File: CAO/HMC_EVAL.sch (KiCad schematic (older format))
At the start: 36 parts, among them U1 OPA2209

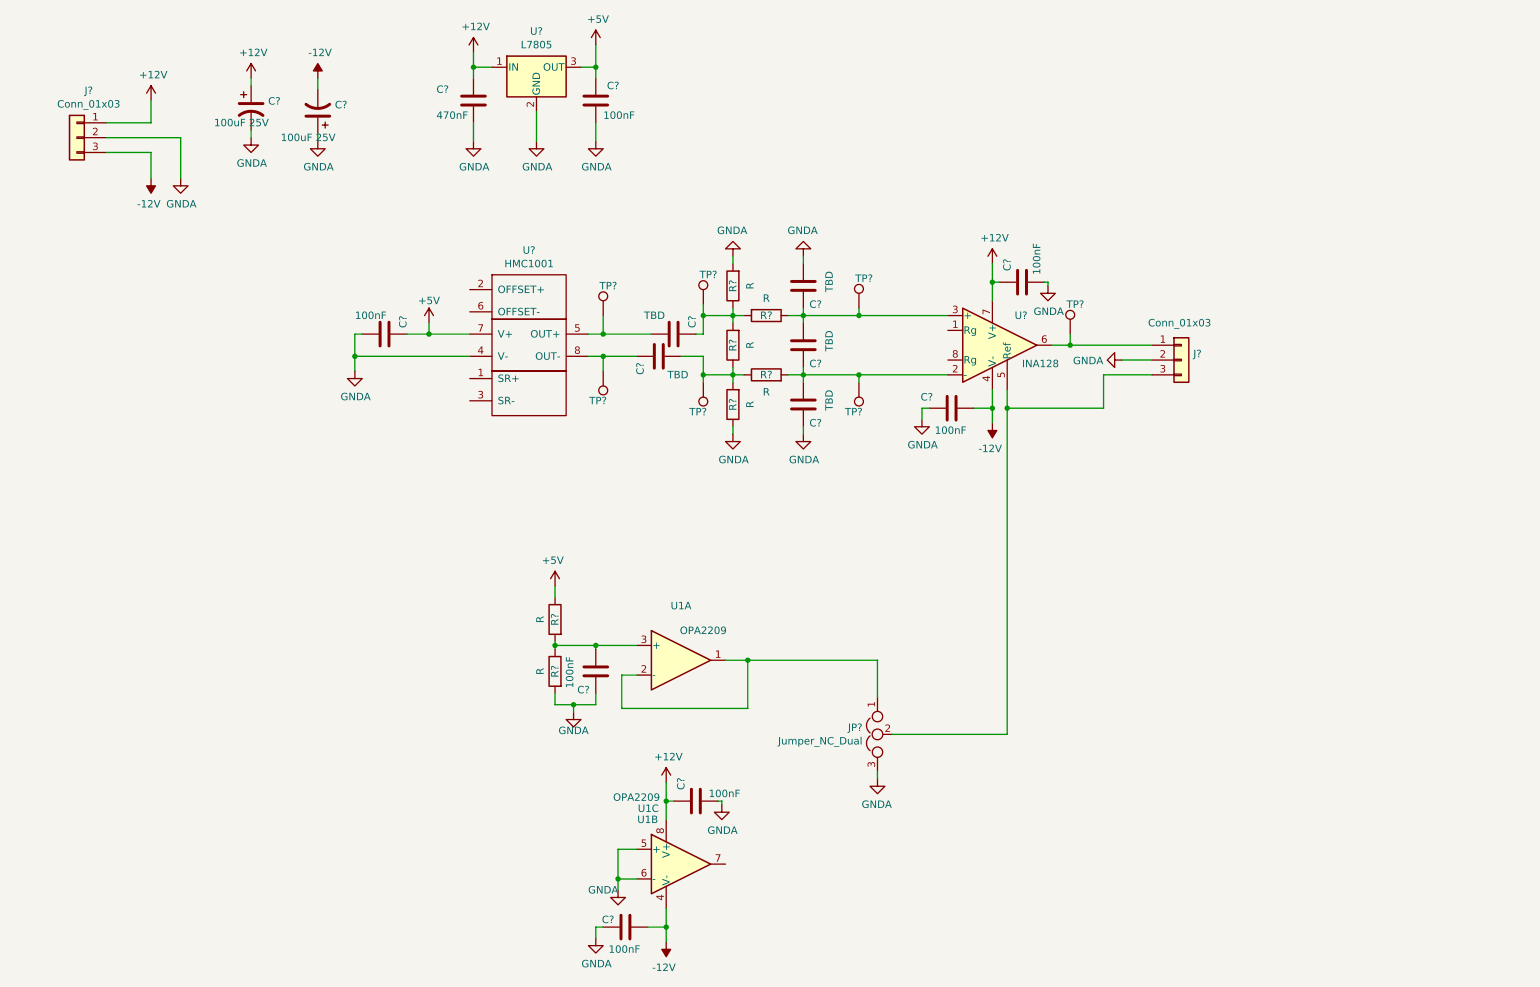
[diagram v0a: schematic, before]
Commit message: Finalisation of schemtic. Probably it's necesary to improve design for low noise with less testPoint and Less configuration.
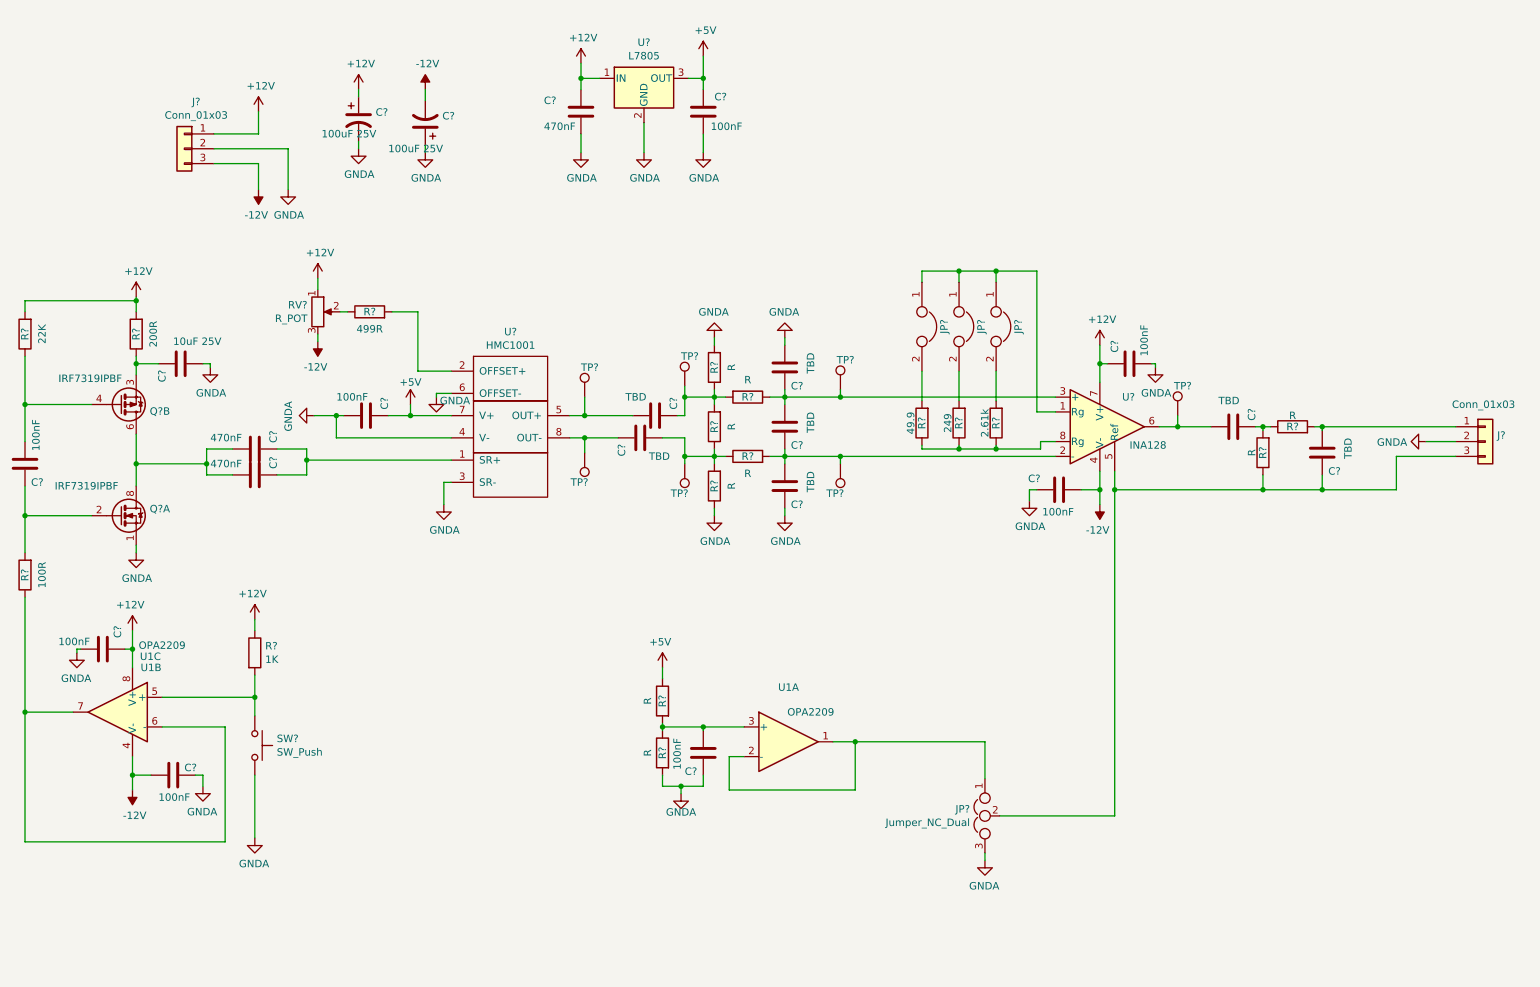
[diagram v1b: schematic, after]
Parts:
- added C? (x2): TBD, Capacitors_SMD:C_0805_HandSoldering, symbol Device:C
- added C? (x2): 470nF, Capacitors_SMD:C_0805_HandSoldering, symbol Device:C
- added C?: 100nF, Capacitors_SMD:C_0805_HandSoldering, symbol Device:C
- added C?: 10uF 25V, Capacitors_SMD:C_1206_HandSoldering, symbol Device:C
- added JP? (x3): Jumper, symbol Device:Jumper
- added Q? (x2): IRF7319IPBF, Package_SO:SOIC-8_3.9x4.9mm_P1.27mm, symbol Transistor_FET:IRF7309IPBF
- added R? (x2): R, Resistors_SMD:R_0805_HandSoldering, symbol Device:R
- added R?: 2.61k, Resistors_SMD:R_0805_HandSoldering, symbol Device:R
- added R?: 249, Resistors_SMD:R_0805_HandSoldering, symbol Device:R
- added R?: 49.9, Resistors_SMD:R_0805_HandSoldering, symbol Device:R
- added R?: 22K, Resistors_SMD:R_0805_HandSoldering, symbol Device:R
- added R?: 200R, Resistors_SMD:R_1206_HandSoldering, symbol Device:R
- added R?: 100R, Resistors_SMD:R_1206_HandSoldering, symbol Device:R
- added R?: 1K, symbol Device:R
- added R?: 499R, Resistors_SMD:R_1206_HandSoldering, symbol Device:R
- added RV?: R_POT, symbol Device:R_POT
- added SW?: SW_Push, symbol Switch:SW_Push
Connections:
- net +12V: now also R?.1, R?.2, R?.2, RV?.1
- net -12V: now also RV?.3
- net GNDA: now also U?.3 (SR-), U?.6 (OFFSET-), C?.2, Q?.1 (S), SW?.2; no longer U1.5 (+), U1.6 (-)
- net at U?.1 (SR+): now also C?.1, C?.1
- net at U?.2 (OFFSET+): now also R?.2
- net at U?.1 (Rg): now also JP?.1, JP?.1, JP?.1
- net at J?.3 (Pin_3), JP?.2, U?.5 (Ref): now also C?.1, R?.1
- net at TP?.1, U?.6: now also C?.2; no longer J?.1 (Pin_1)
- net at U?.8 (Rg): now also R?.1, R?.1, R?.1
- net at U1.7: now also U1.6 (-), R?.1
- new net: JP?.2, R?.2 (x3)
- new net: R?.2, SW?.1, U1.5 (+)
- new net: C?.1, R?.1, R?.2
- new net: C?.2, J?.1 (Pin_1), R?.2
- new net: C?.2, C?.2, Q?.5 (D), Q?.6 (D), Q?.7 (D), Q?.8 (D)
- new net: C?.1, Q?.2 (G), R?.2
- new net: C?.1, Q?.3 (1), R?.1
- new net: C?.2, Q?.4 (G), R?.1
- new net: R?.1, RV?.2
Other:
- moved on the sheet: C?, J?, JP?, R?, TP?, U1A, U1B, U1C, U?

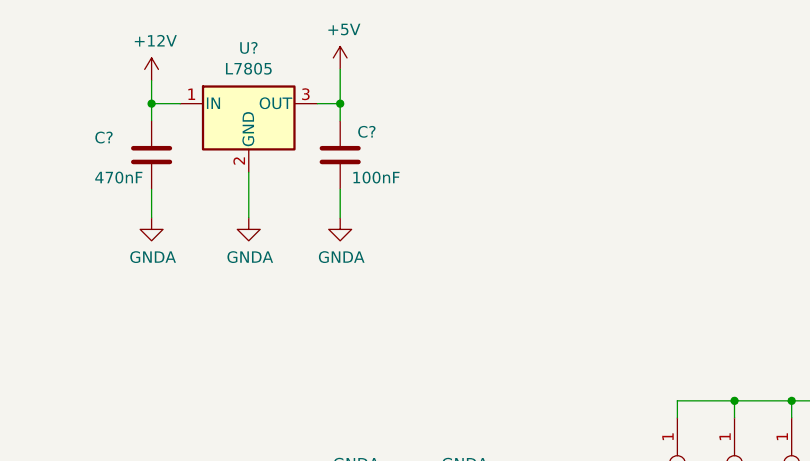
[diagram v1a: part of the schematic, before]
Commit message: Add Gnda TestPoint.
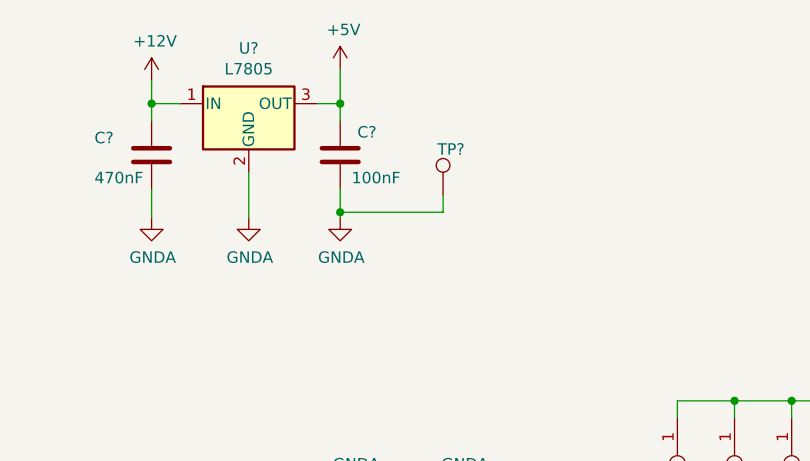
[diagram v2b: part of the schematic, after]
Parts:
- added TP?: TestPoint, symbol Connector:TestPoint
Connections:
- net GNDA: now also TP?.1
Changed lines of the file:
@@
 $EndComp
 Wire Wire Line
-	5350 1450 5350 1325
+	5350 1450 5350 1425
 $Comp
 L power:+5V #PWR?
@@
 Wire Wire Line
 	2750 2725 2750 2675
+$Comp
+L Connector:TestPoint TP?
+U 1 1 5CB304D9
+P 5800 1350
+F 0 "TP?" H 5775 1550 50  0000 L CNN
+F 1 "TestPoint" H 5675 1600 50  0001 L CNN
+F 2 "" H 6000 1350 50  0001 C CNN
+F 3 "~" H 6000 1350 50  0001 C CNN
+	1    5800 1350
+	1    0    0    -1
+$EndComp
+Wire Wire Line
+	5800 1350 5800 1425
+Wire Wire Line
+	5800 1425 5350 1425
+Connection ~ 5350 1425
+Wire Wire Line
+	5350 1425 5350 1325
 $EndSCHEMATC

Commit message: -Suppression of regulator 5V (7805). -Association of components with package.
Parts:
- removed C?: 470nF, symbol Device:C
- removed C?: 100nF, Capacitors_SMD:C_0805_HandSoldering, symbol Device:C
- removed U?: L7805, symbol Regulator_Linear:L7805
- added RV2: R_POT, Potentiometers:Potentiometer_Trimmer_Bourns_3296W, symbol Device:R_POT
- C7, C9: renamed from C?; footprint (none) -> Capacitors_THT:CP_Radial_D10.0mm_P5.00mm
- J1, J2: renamed from J?; footprint (none) -> Connectors_Phoenix:PhoenixContact_MSTBVA-G_03x5.08mm_Vertical
- JP1, JP2, JP4: renamed from JP?; footprint (none) -> Connectors_Samtec:SL-102-X-XX_1x02
- JP3: renamed from JP?; footprint (none) -> Connectors_Samtec:SL-103-X-XX_1x03
- Q1: renamed from Q?; footprint Package_SO:SOIC-8_3.9x4.9mm_P1.27mm -> Housings_SOIC:SOIC-8_3.9x4.9mm_Pitch1.27mm
- R4: renamed from R?; footprint (none) -> Resistors_SMD:R_0805_HandSoldering
- RV1: renamed from RV?; footprint (none) -> Potentiometers:Potentiometer_Trimmer_Bourns_3296W
- SW1: renamed from SW?; footprint (none) -> airsystems:FSM2JSMA
- TP1, TP2, TP3, TP4, TP5, TP6, TP7, TP8: renamed from TP?; footprint (none) -> Connectors_Samtec:SL-101-X-XX_1x01
- U1: footprint (none) -> Housings_SOIC:SOIC-8_3.9x4.9mm_Pitch1.27mm
- U1: value OPA2134 -> OPA2209; footprint (none) -> Housings_SOIC:SOIC-8_3.9x4.9mm_Pitch1.27mm
- U4: renamed from U?; footprint (none) -> Housings_SOIC:SOIC-8_3.9x4.9mm_Pitch1.27mm; supplier (none) -> Farnell: 1206896
- gave numbers to parts that had none: 34
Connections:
- net +12V: now also R6.1
- net +5V: no longer R6.1
- net GNDA: now also RV2.2, RV2.3
- net at C14.2, R6.2, R7.1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: now also RV2.1
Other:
- moved on the sheet: C7, C9, J1, TP5

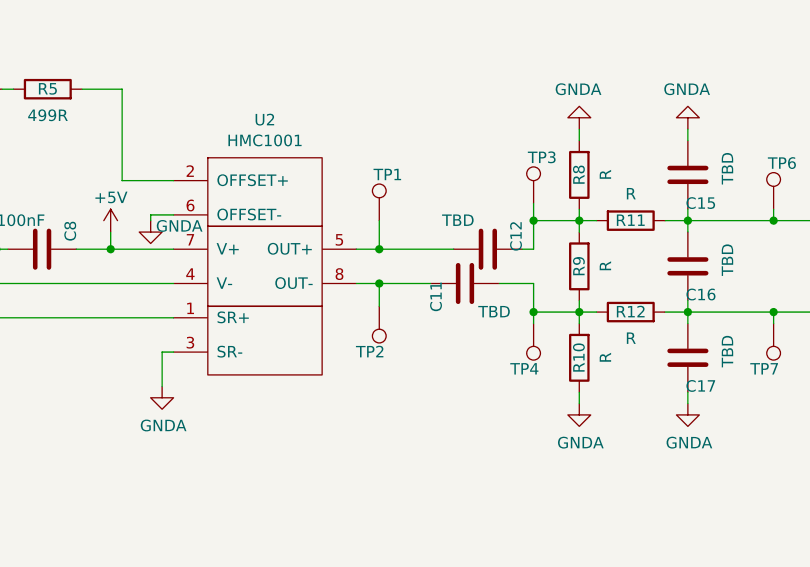
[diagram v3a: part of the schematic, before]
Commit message: Add Library folder for HMC1001.
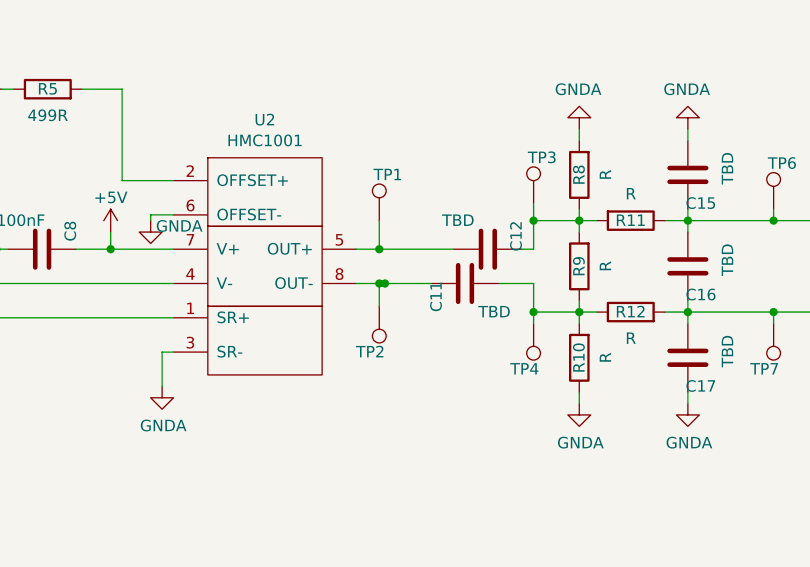
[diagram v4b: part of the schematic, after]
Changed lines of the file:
@@
 Connection ~ 4550 3375
 Wire Wire Line
-	4550 3375 4775 3375
+	4550 3375 4575 3375
 $Comp
 L Connector:TestPoint TP8
@@
 Wire Wire Line
 	4725 5325 4725 5375
+Connection ~ 4575 3375
+Wire Wire Line
+	4575 3375 4775 3375
 $EndSCHEMATC
